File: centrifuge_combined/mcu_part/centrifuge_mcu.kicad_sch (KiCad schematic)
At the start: 16 parts, among them J501 Conn_02x06_Odd_Even, J503 FPGA_extra, J505 FPGA_SPI, J506 DDCI2C2, J507 ADC_I2C, J508 ADC_RST, J516 Conn_02x06_Odd_Even, J517 DDCI2C1, U501 DFR0555, U502 LCD16x2L

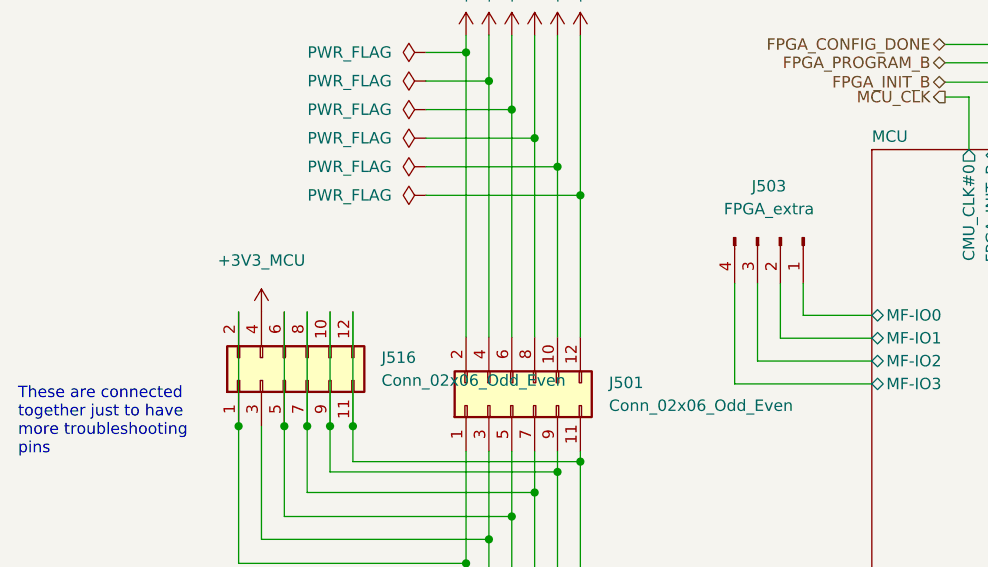
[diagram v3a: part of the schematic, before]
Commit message: Fixed missing footprints, added decoupling capacitors, adjusted board edges
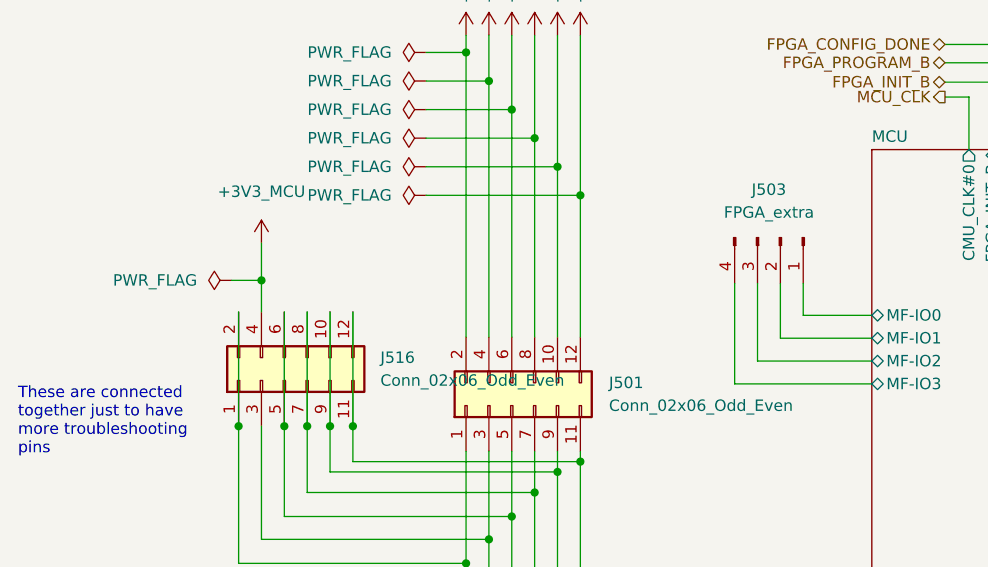
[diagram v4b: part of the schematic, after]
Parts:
- J501: footprint (none) -> Connector_PinHeader_2.54mm:PinHeader_2x06_P2.54mm_Vertical
- J503, J505, U501: footprint (none) -> Connector_PinHeader_2.54mm:PinHeader_1x04_P2.54mm_Vertical
- J507, J508: footprint (none) -> Connector_PinHeader_2.54mm:PinHeader_1x02_P2.54mm_Vertical
- R501, R502, R503, R504, R505, R506: footprint (none) -> Resistor_SMD:R_0805_2012Metric_Pad1.20x1.40mm_HandSolder
- U502: footprint (none) -> centrifuge_mcu:DFR0555
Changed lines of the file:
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@@
     (title "VGA Centrifuge")
     (date "2022-10-03")
-    (rev "R2")
+    (rev "R3")
+    (comment 1 "Author: Håvard Krogstie")
+    (comment 2 "MCU part")
   )
   (junction (at 71.755 60.325) (diameter 0) (color 0 0 0 0)
@@
   (junction (at 199.39 52.705) (diameter 0) (color 0 0 0 0)
   )
+  (junction (at 41.402 76.1238) (diameter 0) (color 0 0 0 0)
+  )
   (junction (at 148.59 52.197) (diameter 0) (color 0 0 0 0)
   )
@@
     (stroke (width 0) (type default) (color 0 0 0 0))
   )
+  (wire (pts (xy 38.0746 76.1238) (xy 41.402 76.1238))
+    (stroke (width 0) (type default) (color 0 0 0 0))
+  )
   (wire (pts (xy 117.348 55.753) (xy 120.015 55.753))
     (stroke (width 0) (type default) (color 0 0 0 0))
@@
     (stroke (width 0) (type default) (color 0 0 0 0))
   )
+  (wire (pts (xy 41.402 71.9836) (xy 41.402 76.1238))
+    (stroke (width 0) (type default) (color 0 0 0 0))
+  )
   (wire (pts (xy 174.625 68.58) (xy 187.325 68.58))
     (stroke (width 0) (type default) (color 0 0 0 0))
   )
   (wire (pts (xy 151.13 33.02) (xy 156.845 33.02))
+    (stroke (width 0) (type default) (color 0 0 0 0))
+  )
+  (wire (pts (xy 41.402 76.1238) (xy 41.402 79.629))
     (stroke (width 0) (type default) (color 0 0 0 0))
   )
@@
     (property "Reference" "R503" (id 0) (at 160.655 40.64 90))
     (property "Value" "2.2k" (id 1) (at 160.655 42.545 90))
-    (property "Footprint" "" (id 2) (at 160.655 44.323 90)
+    (property "Footprint" "Resistor_SMD:R_0805_2012Metric_Pad1.20x1.40mm_HandSolder" (id 2) (at 160.655 44.323 90)
       (effects (font (size 1.27 1.27)) hide)
     )
@@
     (pin "2")
   )
-  (symbol (lib_id "centrifuge_symbols:+3V3_MCU") (at 41.402 79.629 0) (unit 1)
-    (in_bom yes) (on_board yes) (fields_autoplaced)
-    (property "Reference" "#PWR0238" (id 0) (at 41.402 83.439 0)
-      (effects (font (size 1.27 1.27)) hide)
-    )
-    (property "Value" "+3V3_MCU" (id 1) (at 41.402 73.914 0))
-    (property "Footprint" "" (id 2) (at 41.402 79.629 0)
-      (effects (font (size 1.27 1.27)) hide)
-    )
-    (property "Datasheet" "" (id 3) (at 41.402 79.629 0)
+  (symbol (lib_id "centrifuge_symbols:+3V3_MCU") (at 41.402 71.9836 0) (unit 1)
+    (in_bom yes) (on_board yes) (fields_autoplaced)
+    (property "Reference" "#PWR0238" (id 0) (at 41.402 75.7936 0)
+      (effects (font (size 1.27 1.27)) hide)
+    )
+    (property "Value" "+3V3_MCU" (id 1) (at 41.402 66.2686 0))
+    (property "Footprint" "" (id 2) (at 41.402 71.9836 0)
+      (effects (font (size 1.27 1.27)) hide)
+    )
+    (property "Datasheet" "" (id 3) (at 41.402 71.9836 0)
       (effects (font (size 1.27 1.27)) hide)
     )
@@
     (property "Reference" "J505" (id 0) (at 137.795 20.32 90))
     (property "Value" "FPGA_SPI" (id 1) (at 137.795 22.86 90))
-    (property "Footprint" "" (id 2) (at 139.065 26.035 0)
+    (property "Footprint" "Connector_PinHeader_2.54mm:PinHeader_1x04_P2.54mm_Vertical" (id 2) (at 139.065 26.035 0)
       (effects (font (size 1.27 1.27)) hide)
     )
@@
     (property "Reference" "R505" (id 0) (at 176.53 63.5 90))
     (property "Value" "2.2k" (id 1) (at 174.625 63.5 90))
-    (property "Footprint" "" (id 2) (at 172.847 63.5 90)
+    (property "Footprint" "Resistor_SMD:R_0805_2012Metric_Pad1.20x1.40mm_HandSolder" (id 2) (at 172.847 63.5 90)
       (effects (font (size 1.27 1.27)) hide)
     )
@@
     (property "Reference" "R506" (id 0) (at 182.245 63.5 90))
     (property "Value" "2.2k" (id 1) (at 180.34 63.5 90))
-    (property "Footprint" "" (id 2) (at 178.562 63.5 90)
+    (property "Footprint" "Resistor_SMD:R_0805_2012Metric_Pad1.20x1.40mm_HandSolder" (id 2) (at 178.562 63.5 90)
       (effects (font (size 1.27 1.27)) hide)
     )
@@
     (property "Reference" "R504" (id 0) (at 160.655 45.085 90))
     (property "Value" "2.2k" (id 1) (at 160.655 46.99 90))
-    (property "Footprint" "" (id 2) (at 160.655 48.768 90)
+    (property "Footprint" "Resistor_SMD:R_0805_2012Metric_Pad1.20x1.40mm_HandSolder" (id 2) (at 160.655 48.768 90)
       (effects (font (size 1.27 1.27)) hide)
     )
@@
       (effects (font (size 1.27 1.27)) (justify left))
     )
-    (property "Footprint" "" (id 2) (at 264.795 66.675 0)
+    (property "Footprint" "centrifuge_mcu:DFR0555" (id 2) (at 264.795 66.675 0)
       (effects (font (size 1.27 1.27)) hide)
     )
@@
   (symbol (lib_id "Connector:Conn_01x04_Male") (at 99.06 71.374 270) (unit 1)
     (in_bom yes) (on_board yes) (fields_autoplaced)
-    (property "Reference" "J503" (id 0) (at 97.79 65.659 90))
-    (property "Value" "FPGA_extra" (id 1) (at 97.79 68.199 90))
-    (property "Footprint" "" (id 2) (at 99.06 71.374 0)
+    (property "Reference" "J503" (id 0) (at 97.79 66.04 90))
+    (property "Value" "FPGA_extra" (id 1) (at 97.79 68.58 90))
+    (property "Footprint" "Connector_PinHeader_2.54mm:PinHeader_1x04_P2.54mm_Vertical" (id 2) (at 99.06 71.374 0)
       (effects (font (size 1.27 1.27)) hide)
     )
@@
       (effects (font (size 1.27 1.27)) (justify left))
     )
-    (property "Footprint" "" (id 2) (at 243.84 64.135 0)
+    (property "Footprint" "Connector_PinHeader_2.54mm:PinHeader_1x04_P2.54mm_Vertical" (id 2) (at 243.84 64.135 0)
       (effects (font (size 1.27 1.27)) hide)
     )
@@
     (pin "3")
     (pin "4")
+  )
+  (symbol (lib_id "power:PWR_FLAG") (at 38.0746 76.1238 90) (unit 1)
+    (in_bom yes) (on_board yes) (fields_autoplaced)
+    (property "Reference" "#FLG0509" (id 0) (at 36.1696 76.1238 0)
+      (effects (font (size 1.27 1.27)) hide)
+    )
+    (property "Value" "PWR_FLAG" (id 1) (at 34.2646 76.1237 90)
+      (effects (font (size 1.27 1.27)) (justify left))
+    )
+    (property "Footprint" "" (id 2) (at 38.0746 76.1238 0)
+      (effects (font (size 1.27 1.27)) hide)
+    )
+    (property "Datasheet" "~" (id 3) (at 38.0746 76.1238 0)
+      (effects (font (size 1.27 1.27)) hide)
+    )
+    (pin "1")
   )
   (symbol (lib_id "Connector:Conn_01x02_Male") (at 151.13 26.0096 270) (unit 1)
@@
       (effects (font (size 1.27 1.27)) (justify left))
     )
-    (property "Footprint" "" (id 2) (at 189.865 25.4 0)
+    (property "Footprint" "Connector_PinHeader_2.54mm:PinHeader_1x02_P2.54mm_Vertical" (id 2) (at 189.865 25.4 0)
       (effects (font (size 1.27 1.27)) hide)
     )
@@
   (symbol (lib_id "Connector_Generic:Conn_02x06_Odd_Even") (at 43.942 87.249 90) (unit 1)
     (in_bom yes) (on_board yes) (fields_autoplaced)
-    (property "Reference" "J516" (id 0) (at 54.737 84.7089 90)
+    (property "Reference" "J516" (id 0) (at 54.61 84.7089 90)
       (effects (font (size 1.27 1.27)) (justify right))
     )
-    (property "Value" "Conn_02x06_Odd_Even" (id 1) (at 54.737 87.2489 90)
+    (property "Value" "Conn_02x06_Odd_Even" (id 1) (at 54.61 87.2489 90)
       (effects (font (size 1.27 1.27)) (justify right))
     )
@@
       (effects (font (size 1.27 1.27)) (justify right))
     )
-    (property "Footprint" "" (id 2) (at 69.215 90.043 0)
+    (property "Footprint" "Connector_PinHeader_2.54mm:PinHeader_2x06_P2.54mm_Vertical" (id 2) (at 69.215 90.043 0)
       (effects (font (size 1.27 1.27)) hide)
     )
@@
       (effects (font (size 1.27 1.27)) (justify left))
     )
-    (property "Footprint" "" (id 2) (at 196.85 24.765 0)
+    (property "Footprint" "Connector_PinHeader_2.54mm:PinHeader_1x02_P2.54mm_Vertical" (id 2) (at 196.85 24.765 0)
       (effects (font (size 1.27 1.27)) hide)
     )
@@
     (property "Reference" "R501" (id 0) (at 160.655 31.115 90))
     (property "Value" "2.2k" (id 1) (at 160.655 33.02 90))
-    (property "Footprint" "" (id 2) (at 160.655 34.798 90)
+    (property "Footprint" "Resistor_SMD:R_0805_2012Metric_Pad1.20x1.40mm_HandSolder" (id 2) (at 160.655 34.798 90)
       (effects (font (size 1.27 1.27)) hide)
     )
@@
     (property "Reference" "R502" (id 0) (at 160.655 35.56 90))
     (property "Value" "2.2k" (id 1) (at 160.655 37.465 90))
-    (property "Footprint" "" (id 2) (at 160.655 39.243 90)
-      (effects (font (size 1.27 1.27)) hide)
-    )
+    (property "Footprint" "Resistor_SMD:R_0805_2012Metric_Pad1.20x1.40mm_HandSolder" (id 2) (at 160.655 39.243 90)
+      (effects (font (size 1.27 1.27)) hide)
+    )

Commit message: remove digikey links to products that we already buy from mouser, add mouser link instead
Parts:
- R501, R502, R503, R504, R505, R506: Order Page (none) -> https://no.mouser.com/ProductDetail/Vishay-Dale/CRCW08052K2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; Purchase https://www.digikey.no/no/products/detail/yageo/AC0805FR-07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 -> (none)
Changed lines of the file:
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@@
       (effects (font (size 1.27 1.27)) hide)
     )
-    (property "Purchase" "https://www.digikey.no/no/products/detail/yageo/AC0805FR-072K2L/5896727" (id 4) (at 160.655 42.545 0)
+    (property "Purchase" "" (id 4) (at 160.655 42.545 0)
+      (effects (font (size 1.27 1.27)) hide)
+    )
+    (property "Order Page" "https://no.mouser.com/ProductDetail/Vishay-Dale/CRCW08052K20FKEB?qs=sGAEpiMZZMtlubZbdhIBINvvmcV35a3LmL3hFYkil7g%3D" (id 5) (at 160.655 42.545 0)
       (effects (font (size 1.27 1.27)) hide)
     )
@@
       (effects (font (size 1.27 1.27)) hide)
     )
-    (property "Purchase" "https://www.digikey.no/no/products/detail/yageo/AC0805FR-072K2L/5896727" (id 4) (at 174.625 63.5 0)
+    (property "Purchase" "" (id 4) (at 174.625 63.5 0)
+      (effects (font (size 1.27 1.27)) hide)
+    )
+    (property "Order Page" "https://no.mouser.com/ProductDetail/Vishay-Dale/CRCW08052K20FKEB?qs=sGAEpiMZZMtlubZbdhIBINvvmcV35a3LmL3hFYkil7g%3D" (id 5) (at 174.625 63.5 0)
       (effects (font (size 1.27 1.27)) hide)
     )
@@
       (effects (font (size 1.27 1.27)) hide)
     )
-    (property "Purchase" "https://www.digikey.no/no/products/detail/yageo/AC0805FR-072K2L/5896727" (id 4) (at 180.34 63.5 0)
+    (property "Purchase" "" (id 4) (at 180.34 63.5 0)
+      (effects (font (size 1.27 1.27)) hide)
+    )
+    (property "Order Page" "https://no.mouser.com/ProductDetail/Vishay-Dale/CRCW08052K20FKEB?qs=sGAEpiMZZMtlubZbdhIBINvvmcV35a3LmL3hFYkil7g%3D" (id 5) (at 180.34 63.5 0)
       (effects (font (size 1.27 1.27)) hide)
     )
@@
       (effects (font (size 1.27 1.27)) hide)
     )
-    (property "Purchase" "https://www.digikey.no/no/products/detail/yageo/AC0805FR-072K2L/5896727" (id 4) (at 160.655 46.99 0)
+    (property "Purchase" "" (id 4) (at 160.655 46.99 0)
+      (effects (font (size 1.27 1.27)) hide)
+    )
+    (property "Order Page" "https://no.mouser.com/ProductDetail/Vishay-Dale/CRCW08052K20FKEB?qs=sGAEpiMZZMtlubZbdhIBINvvmcV35a3LmL3hFYkil7g%3D" (id 5) (at 160.655 46.99 0)
       (effects (font (size 1.27 1.27)) hide)
     )
@@
       (effects (font (size 1.27 1.27)) hide)
     )
-    (property "Purchase" "https://www.digikey.no/no/products/detail/yageo/AC0805FR-072K2L/5896727" (id 4) (at 160.655 33.02 0)
+    (property "Purchase" "" (id 4) (at 160.655 33.02 0)
+      (effects (font (size 1.27 1.27)) hide)
+    )
+    (property "Order Page" "https://no.mouser.com/ProductDetail/Vishay-Dale/CRCW08052K20FKEB?qs=sGAEpiMZZMtlubZbdhIBINvvmcV35a3LmL3hFYkil7g%3D" (id 5) (at 160.655 33.02 0)
       (effects (font (size 1.27 1.27)) hide)
     )
@@
       (effects (font (size 1.27 1.27)) hide)
     )
-    (property "Purchase" "https://www.digikey.no/no/products/detail/yageo/AC0805FR-072K2L/5896727" (id 4) (at 160.655 37.465 0)
-      (effects (font (size 1.27 1.27)) hide)
-    )
+    (property "Purchase" "" (id 4) (at 160.655 37.465 0)
+      (effects (font (size 1.27 1.27)) hide)
+    )
+    (property "Order Page" "https://no.mouser.com/ProductDetail/Vishay-Dale/CRCW08052K20FKEB?qs=sGAEpiMZZMtlubZbdhIBINvvmcV35a3LmL3hFYkil7g%3D" (id 5) (at 160.655 37.465 0)
+      (effects (font (size 1.27 1.27)) hide)
+    )

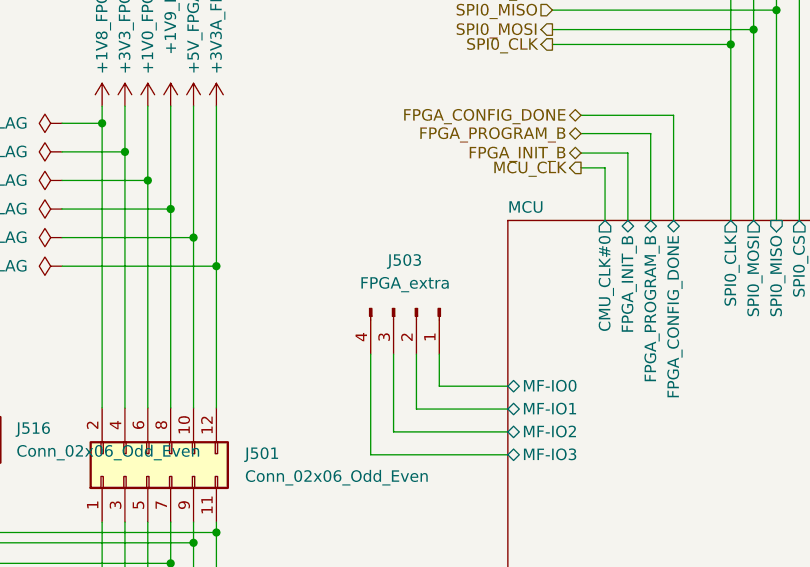
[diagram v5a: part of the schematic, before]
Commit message: fix elprint complaints, except intranet clearance, also widen some traces
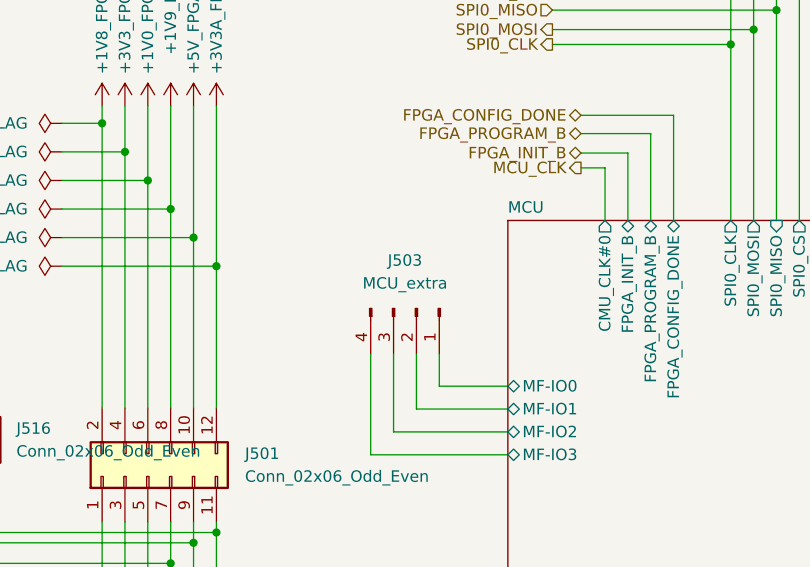
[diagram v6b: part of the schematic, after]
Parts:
- J503: value FPGA_extra -> MCU_extra
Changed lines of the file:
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@@
     (in_bom yes) (on_board yes) (fields_autoplaced)
     (property "Reference" "J503" (id 0) (at 97.79 66.04 90))
-    (property "Value" "FPGA_extra" (id 1) (at 97.79 68.58 90))
+    (property "Value" "MCU_extra" (id 1) (at 97.79 68.58 90))
     (property "Footprint" "Connector_PinHeader_2.54mm:PinHeader_1x04_P2.54mm_Vertical" (id 2) (at 99.06 71.374 0)
       (effects (font (size 1.27 1.27)) hide)

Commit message: Fixed Elprint complaints and JTAG VREF problems+config flash CS
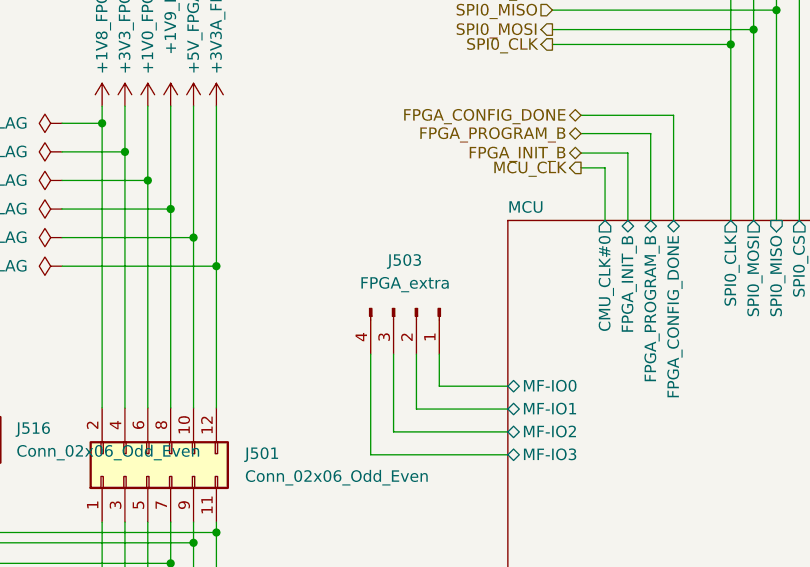
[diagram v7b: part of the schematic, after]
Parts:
- J503: value MCU_extra -> FPGA_extra
- R501, R502, R503, R504, R505, R506: Order Page https://no.mouser.com/ProductDetail/Vishay-Dale/CRCW08052K2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 -> (none); Purchase (none) -> https://www.digikey.no/no/products/detail/yageo/AC0805FR-07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
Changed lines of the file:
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@@
   (title_block
     (title "VGA Centrifuge")
-    (date "2022-10-03")
-    (rev "R3")
+    (date "2022-10-05")
+    (rev "R4")
     (comment 1 "Author: Håvard Krogstie")
     (comment 2 "MCU part")
@@
       (effects (font (size 1.27 1.27)) hide)
     )
-    (property "Purchase" "" (id 4) (at 160.655 42.545 0)
-      (effects (font (size 1.27 1.27)) hide)
-    )
-    (property "Order Page" "https://no.mouser.com/ProductDetail/Vishay-Dale/CRCW08052K20FKEB?qs=sGAEpiMZZMtlubZbdhIBINvvmcV35a3LmL3hFYkil7g%3D" (id 5) (at 160.655 42.545 0)
+    (property "Purchase" "https://www.digikey.no/no/products/detail/yageo/AC0805FR-072K2L/5896727" (id 4) (at 160.655 42.545 0)
       (effects (font (size 1.27 1.27)) hide)
     )
@@
       (effects (font (size 1.27 1.27)) hide)
     )
-    (property "Purchase" "" (id 4) (at 174.625 63.5 0)
-      (effects (font (size 1.27 1.27)) hide)
-    )
-    (property "Order Page" "https://no.mouser.com/ProductDetail/Vishay-Dale/CRCW08052K20FKEB?qs=sGAEpiMZZMtlubZbdhIBINvvmcV35a3LmL3hFYkil7g%3D" (id 5) (at 174.625 63.5 0)
+    (property "Purchase" "https://www.digikey.no/no/products/detail/yageo/AC0805FR-072K2L/5896727" (id 4) (at 174.625 63.5 0)
       (effects (font (size 1.27 1.27)) hide)
     )
@@
       (effects (font (size 1.27 1.27)) hide)
     )
-    (property "Purchase" "" (id 4) (at 180.34 63.5 0)
-      (effects (font (size 1.27 1.27)) hide)
-    )
-    (property "Order Page" "https://no.mouser.com/ProductDetail/Vishay-Dale/CRCW08052K20FKEB?qs=sGAEpiMZZMtlubZbdhIBINvvmcV35a3LmL3hFYkil7g%3D" (id 5) (at 180.34 63.5 0)
+    (property "Purchase" "https://www.digikey.no/no/products/detail/yageo/AC0805FR-072K2L/5896727" (id 4) (at 180.34 63.5 0)
       (effects (font (size 1.27 1.27)) hide)
     )
@@
       (effects (font (size 1.27 1.27)) hide)
     )
-    (property "Purchase" "" (id 4) (at 160.655 46.99 0)
-      (effects (font (size 1.27 1.27)) hide)
-    )
-    (property "Order Page" "https://no.mouser.com/ProductDetail/Vishay-Dale/CRCW08052K20FKEB?qs=sGAEpiMZZMtlubZbdhIBINvvmcV35a3LmL3hFYkil7g%3D" (id 5) (at 160.655 46.99 0)
+    (property "Purchase" "https://www.digikey.no/no/products/detail/yageo/AC0805FR-072K2L/5896727" (id 4) (at 160.655 46.99 0)
       (effects (font (size 1.27 1.27)) hide)
     )
@@
     (in_bom yes) (on_board yes) (fields_autoplaced)
     (property "Reference" "J503" (id 0) (at 97.79 66.04 90))
-    (property "Value" "MCU_extra" (id 1) (at 97.79 68.58 90))
+    (property "Value" "FPGA_extra" (id 1) (at 97.79 68.58 90))
     (property "Footprint" "Connector_PinHeader_2.54mm:PinHeader_1x04_P2.54mm_Vertical" (id 2) (at 99.06 71.374 0)
       (effects (font (size 1.27 1.27)) hide)
@@
       (effects (font (size 1.27 1.27)) hide)
     )
-    (property "Purchase" "" (id 4) (at 160.655 33.02 0)
-      (effects (font (size 1.27 1.27)) hide)
-    )
-    (property "Order Page" "https://no.mouser.com/ProductDetail/Vishay-Dale/CRCW08052K20FKEB?qs=sGAEpiMZZMtlubZbdhIBINvvmcV35a3LmL3hFYkil7g%3D" (id 5) (at 160.655 33.02 0)
+    (property "Purchase" "https://www.digikey.no/no/products/detail/yageo/AC0805FR-072K2L/5896727" (id 4) (at 160.655 33.02 0)
       (effects (font (size 1.27 1.27)) hide)
     )
@@
       (effects (font (size 1.27 1.27)) hide)
     )
-    (property "Purchase" "" (id 4) (at 160.655 37.465 0)
-      (effects (font (size 1.27 1.27)) hide)
-    )
-    (property "Order Page" "https://no.mouser.com/ProductDetail/Vishay-Dale/CRCW08052K20FKEB?qs=sGAEpiMZZMtlubZbdhIBINvvmcV35a3LmL3hFYkil7g%3D" (id 5) (at 160.655 37.465 0)
-      (effects (font (size 1.27 1.27)) hide)
-    )
+    (property "Purchase" "https://www.digikey.no/no/products/detail/yageo/AC0805FR-072K2L/5896727" (id 4) (at 160.655 37.465 0)
+      (effects (font (size 1.27 1.27)) hide)
+    )
